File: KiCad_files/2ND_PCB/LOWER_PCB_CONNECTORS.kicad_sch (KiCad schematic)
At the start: 3 parts, among them J1 Conn_01x04_Socket, J2 Conn_01x04_Socket, J3 Conn_01x04_Socket

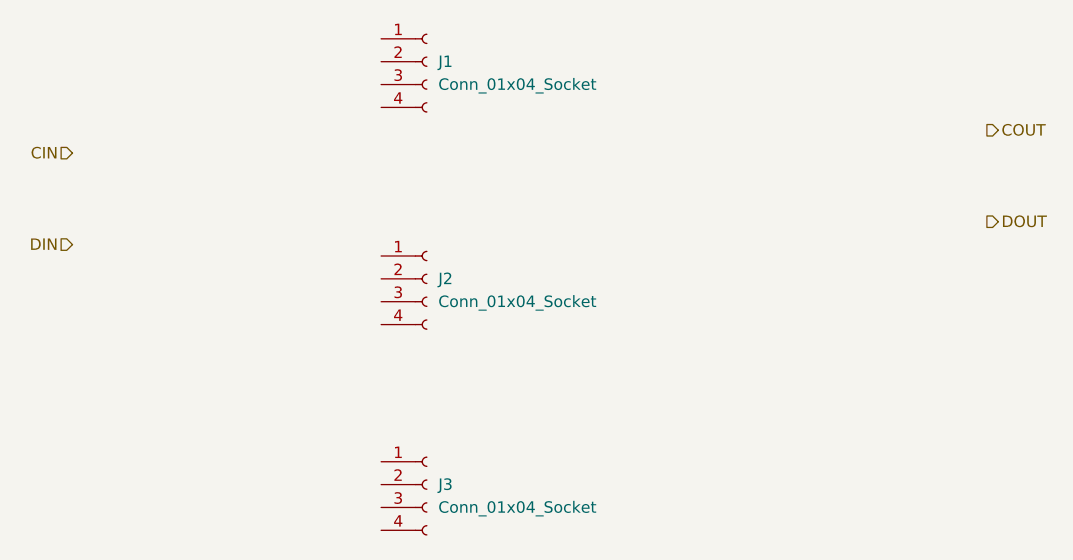
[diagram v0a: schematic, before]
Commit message: Add files via upload
28/8 22:47 -
fixed most errors, still 4 left
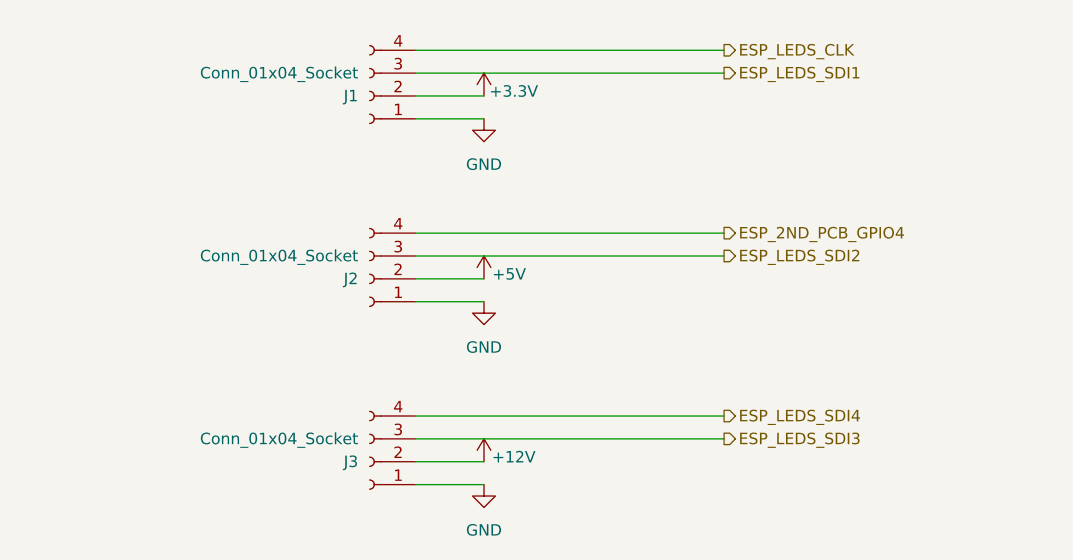
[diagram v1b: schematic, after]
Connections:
- net GND: now reaches J2.1 (Pin_1)
- net GND: now also J1.1 (Pin_1), J3.1 (Pin_1)
- net +5V: now reaches J2.2 (Pin_2)
- net ESP_LEDS_SDI2: now reaches J2.3 (Pin_3)
- net ESP_2ND_PCB_GPIO4: now reaches J2.4 (Pin_4)
- net +12V: now reaches J3.2 (Pin_2)
- net ESP_LEDS_SDI3: now reaches J3.3 (Pin_3)
- net ESP_LEDS_SDI4: now reaches J3.4 (Pin_4)
- net +3.3V: now reaches J1.2 (Pin_2)
- net ESP_LEDS_SDI1: now reaches J1.3 (Pin_3)
- net ESP_LEDS_CLK: now reaches J1.4 (Pin_4)
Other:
- moved on the sheet: J1
